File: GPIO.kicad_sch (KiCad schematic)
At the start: 12 parts, among them J10 Conn_01x03_Pin, J11 Conn_01x03_Pin, J12 Conn_01x04_Pin, J13 Conn_01x04_Pin, J14 Conn_01x03_Pin, J7 Conn_01x04_Pin, J8 Conn_01x03_Pin, J9 Conn_01x04_Pin, U10 D3V3XA4B10LP, U11 D3V3XA4B10LP, U12 D3V3XA4B10LP, U9 D3V3XA4B10LP

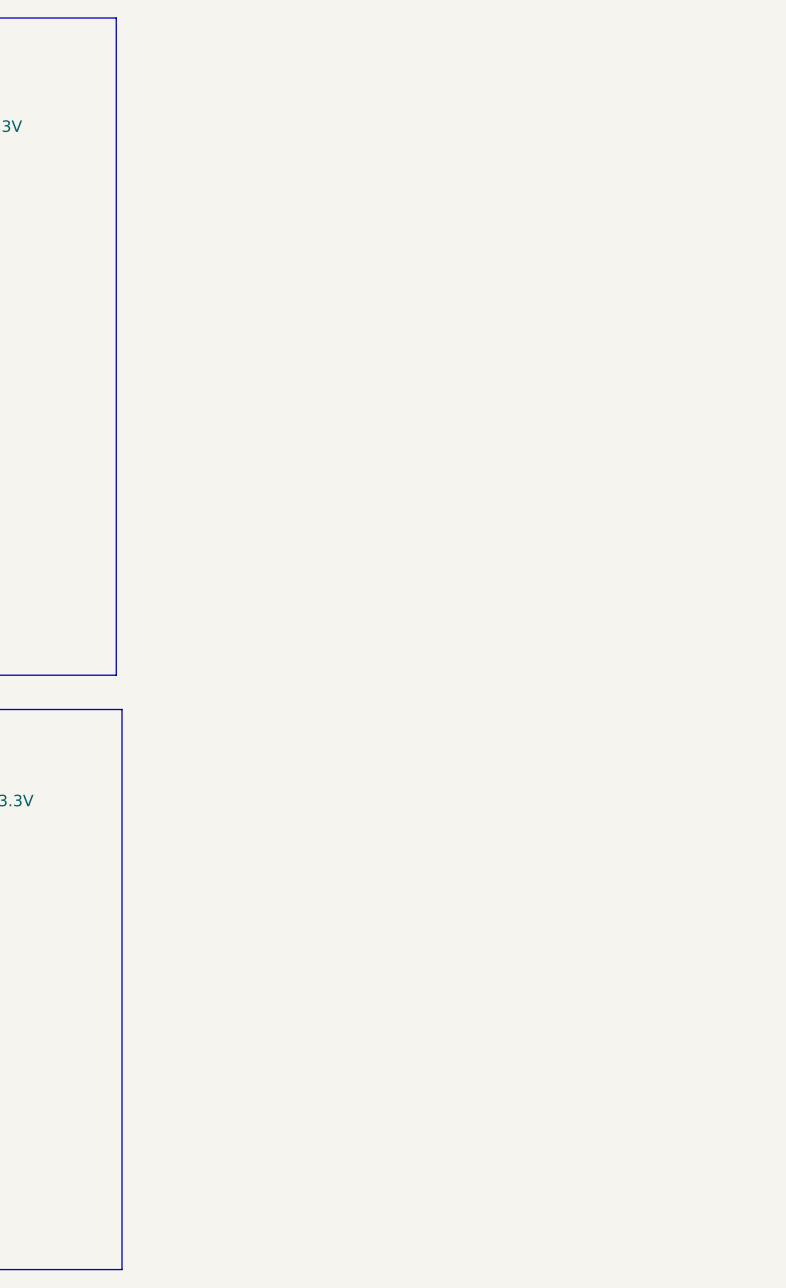
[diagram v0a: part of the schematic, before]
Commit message: Completed GPIO schematic
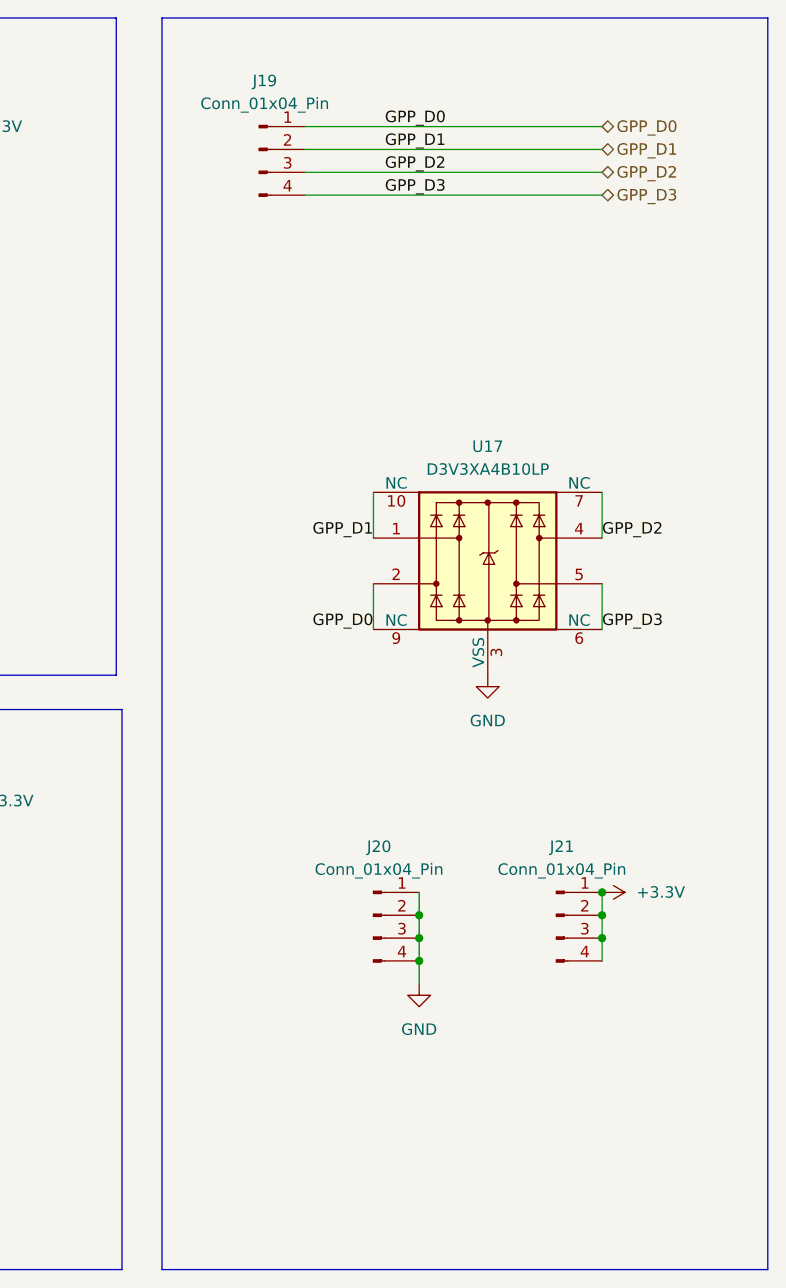
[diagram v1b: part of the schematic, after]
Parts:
- added J19, J20, J21: Conn_01x04_Pin, A_HDJ_Library:PinHeader_1x04_P2.54mm_Vertical, symbol Connector:Conn_01x04_Pin
- added U17: D3V3XA4B10LP, Package_DFN_QFN:Diodes_UDFN-10_1x2.5mm_P0.5mm, symbol Power_Protection:D3V3XA4B10LP
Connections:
- net +3.3V: now also J21.1 (Pin_1), J21.2 (Pin_2), J21.3 (Pin_3), J21.4 (Pin_4)
- net GND: now also J20.1 (Pin_1), J20.2 (Pin_2), J20.3 (Pin_3), J20.4 (Pin_4), U17.3 (VSS), U17.8 (VSS)
- new net GPP_D0: J19.1 (Pin_1), U17.2, U17.9 (NC)
- new net GPP_D1: J19.2 (Pin_2), U17.1, U17.10 (NC)
- new net GPP_D2: J19.3 (Pin_3), U17.4, U17.7 (NC)
- new net GPP_D3: J19.4 (Pin_4), U17.5, U17.6 (NC)

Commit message: Freed up some panda module labels for the wifi/bluetooth chip, and also organized the routes for the gpio connectors into blue layer 2 bundals... not fully connected yet
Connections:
- net GPP_D0: now also U17.1, U17.10 (NC); no longer U17.2, U17.9 (NC)
- net GPP_D1: now also U17.2, U17.9 (NC); no longer U17.1, U17.10 (NC)
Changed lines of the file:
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@@
+	(wire
+		(pts
+			(xy 226.06 86.36) (xy 226.06 91.44)
+		)
+		(stroke
+			(width 0)
+			(type default)
+		)
+	)
 	(wire
 		(pts
@@
 	(wire
 		(pts
-			(xy 226.06 86.36) (xy 226.06 91.44)
-		)
-		(stroke
-			(width 0)
-			(type default)
-		)
-	)
-	(wire
-		(pts
 			(xy 231.14 120.65) (xy 231.14 123.19)
 		)
@@
 	(wire
 		(pts
+			(xy 158.75 113.03) (xy 158.75 115.57)
+		)
+		(stroke
+			(width 0)
+			(type default)
+		)
+	)
+	(wire
+		(pts
+			(xy 95.25 39.37) (xy 128.27 39.37)
+		)
+		(stroke
+			(width 0)
+			(type default)
+		)
+	)
+	(wire
+		(pts
+			(xy 226.06 76.2) (xy 226.06 81.28)
+		)
+		(stroke
+			(width 0)
+			(type default)
+		)
+	)
+	(wire
+		(pts
+			(xy 251.46 120.65) (xy 251.46 123.19)
+		)
+		(stroke
+			(width 0)
+			(type default)
+		)
+	)
+	(wire
+		(pts
+			(xy 33.02 110.49) (xy 58.42 110.49)
+		)
+		(stroke
+			(width 0)
+			(type default)
+		)
+	)
+	(wire
+		(pts
+			(xy 177.8 35.56) (xy 177.8 38.1)
+		)
+		(stroke
+			(width 0)
+			(type default)
+		)
+	)
+	(wire
+		(pts
+			(xy 218.44 35.56) (xy 251.46 35.56)
+		)
+		(stroke
+			(width 0)
+			(type default)
+		)
+	)
+	(wire
+		(pts
+			(xy 68.58 132.08) (xy 68.58 137.16)
+		)
+		(stroke
+			(width 0)
+			(type default)
+		)
+	)
+	(wire
+		(pts
 			(xy 251.46 86.36) (xy 251.46 91.44)
-		)
-		(stroke
-			(width 0)
-			(type default)
-		)
-	)
-	(wire
-		(pts
-			(xy 158.75 113.03) (xy 158.75 115.57)
-		)
-		(stroke
-			(width 0)
-			(type default)
-		)
-	)
-	(wire
-		(pts
-			(xy 95.25 39.37) (xy 128.27 39.37)
-		)
-		(stroke
-			(width 0)
-			(type default)
-		)
-	)
-	(wire
-		(pts
-			(xy 251.46 120.65) (xy 251.46 123.19)
-		)
-		(stroke
-			(width 0)
-			(type default)
-		)
-	)
-	(wire
-		(pts
-			(xy 33.02 110.49) (xy 58.42 110.49)
-		)
-		(stroke
-			(width 0)
-			(type default)
-		)
-	)
-	(wire
-		(pts
-			(xy 177.8 35.56) (xy 177.8 38.1)
-		)
-		(stroke
-			(width 0)
-			(type default)
-		)
-	)
-	(wire
-		(pts
-			(xy 226.06 76.2) (xy 226.06 81.28)
-		)
-		(stroke
-			(width 0)
-			(type default)
-		)
-	)
-	(wire
-		(pts
-			(xy 218.44 35.56) (xy 251.46 35.56)
-		)
-		(stroke
-			(width 0)
-			(type default)
-		)
-	)
-	(wire
-		(pts
-			(xy 68.58 132.08) (xy 68.58 137.16)
 		)
 		(stroke
@@
 	)
 	(label "GPP_D0"
-		(at 226.06 91.44 180)
+		(at 226.06 81.28 180)
 		(effects
 			(font
@@
 	)
 	(label "GPP_D3"
-		(at 251.46 91.44 0)
+		(at 251.46 86.36 0)
 		(effects
 			(font
@@
 	)
 	(label "GPP_D1"
-		(at 226.06 81.28 180)
-		(effects
-			(font
+		(at 226.06 86.36 180)
+		(effects
+			(font
